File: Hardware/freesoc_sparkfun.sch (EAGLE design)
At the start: 94 parts, among them J1 POWER_JACKPTH, U1 CY8C5868AXI-LP035, U2 MIC5219 5V, U3 MIC5219 3.3V, U7 CY8C5868LTI-LP039, Y1 32.768kHz

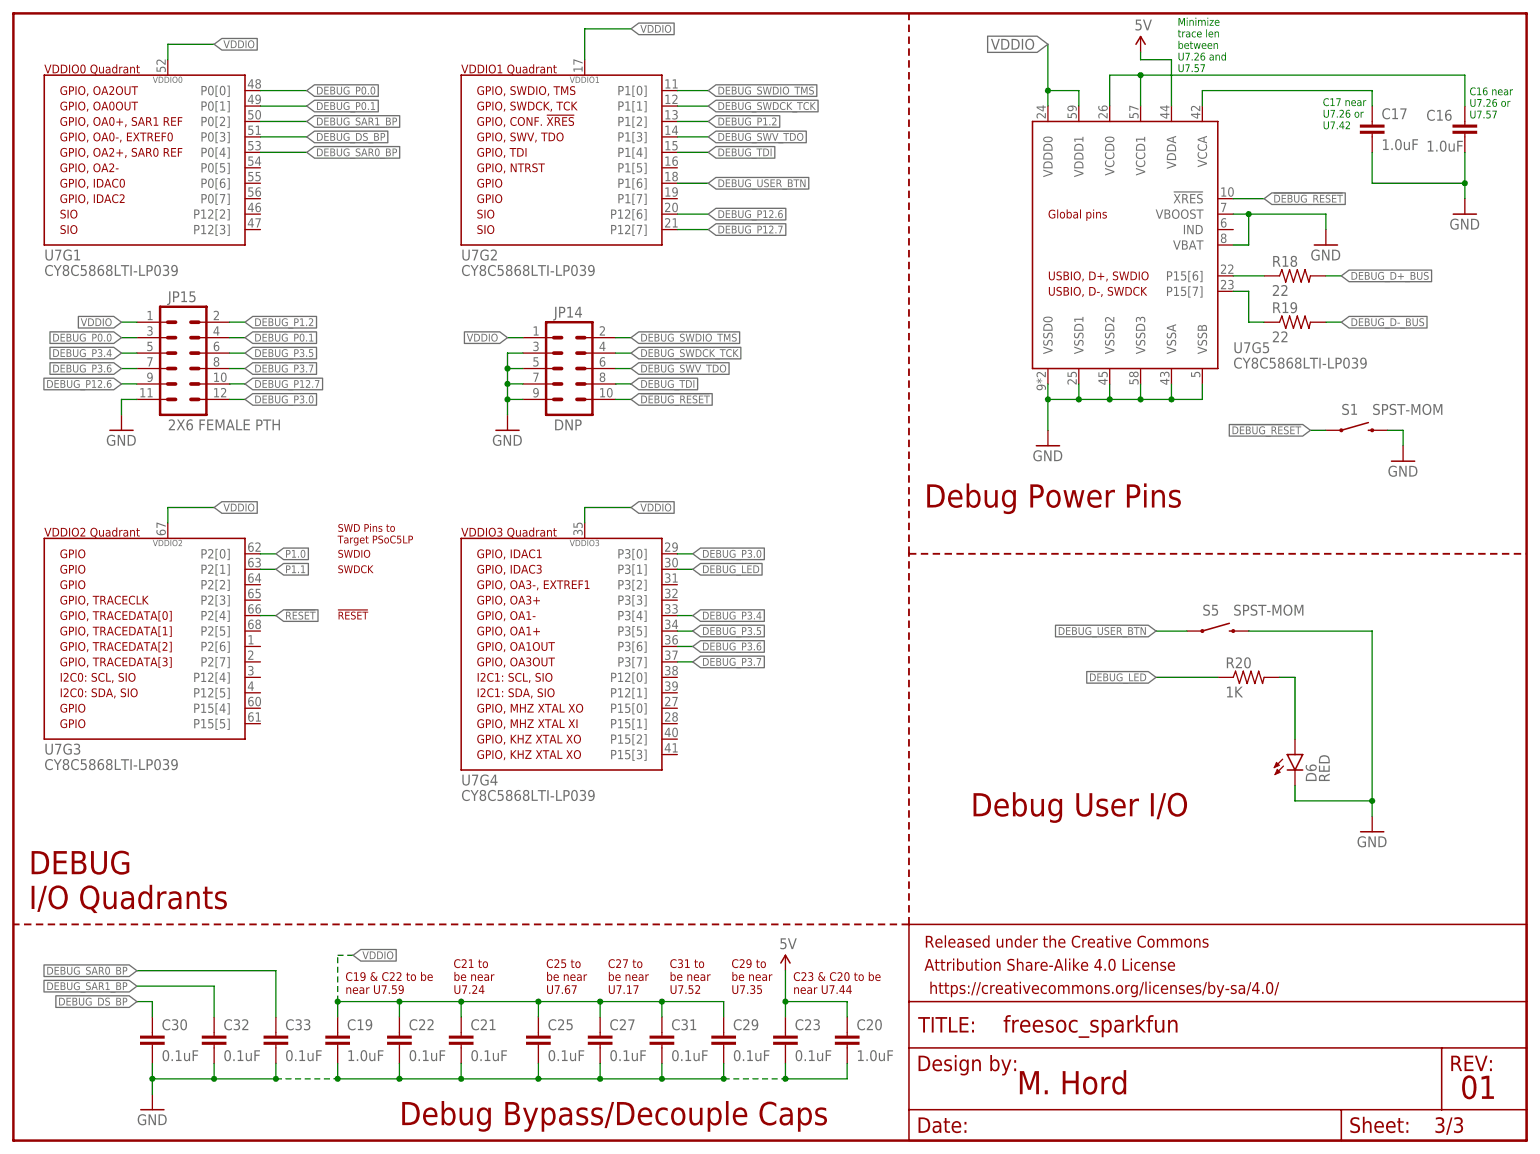
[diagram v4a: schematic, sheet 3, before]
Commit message: Files changed after v01 feedback, to add kitprog ID pins
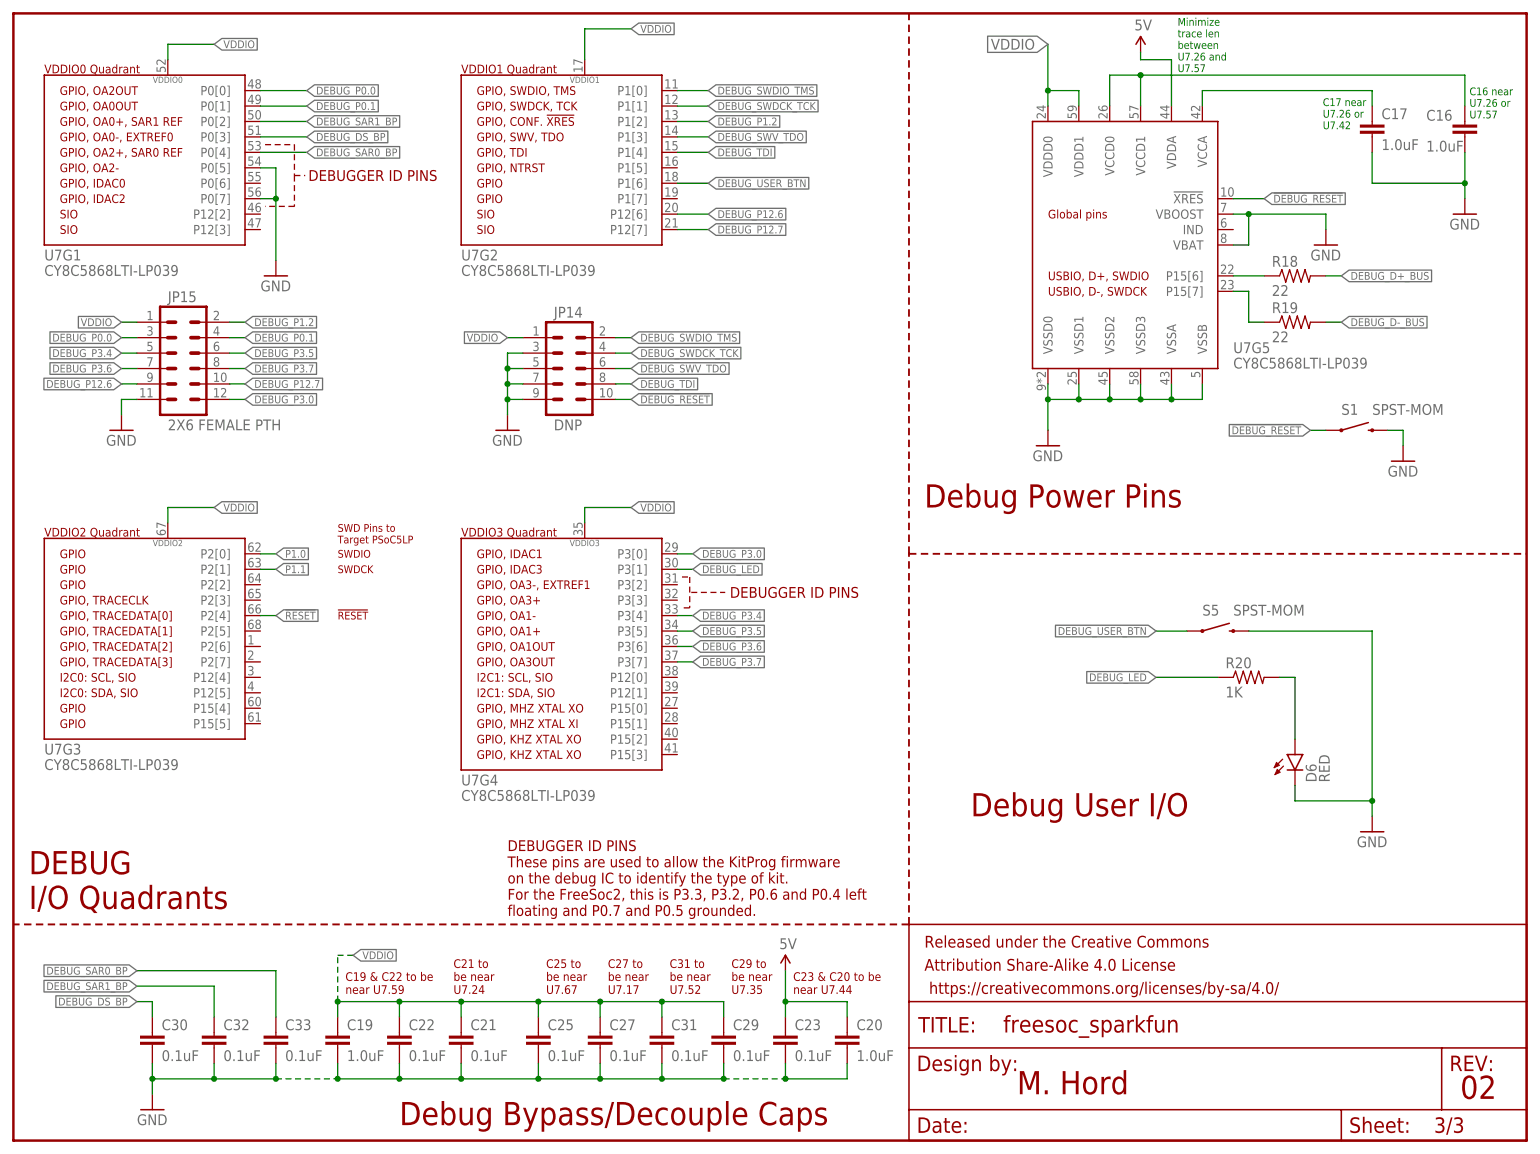
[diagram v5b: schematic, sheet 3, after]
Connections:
- net GND: now also U7G1.P0[5], U7G1.P0[7]
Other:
- note added: "02"
- note added: "DEBUGGER ID PINS"
- note added: "DEBUGGER ID PINS These pins are used to allow the KitProg firmware on the debug IC to identify the type of kit. For the FreeSoc2, this is P3.3, P3.2, P0.6 and P0.4 left floating and P0.7 and P0.5 grounded."
- note removed: "01"
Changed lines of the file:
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@@
 <part name="LOGO2" library="SparkFun-Aesthetics" deviceset="OSHW-LOGO" device="S"/>
 <part name="GND12" library="SparkFun-Aesthetics" deviceset="GND" device=""/>
+<part name="GND28" library="SparkFun-Aesthetics" deviceset="GND" device=""/>
 </parts>
 <sheets>
@@
 <text x="113.792" y="31.496" size="2.54" layer="94">Port 12 (SIO pins)</text>
 <text x="165.1" y="7.62" size="3.81" layer="94">M. Hord</text>
-<text x="237.998" y="6.858" size="3.81" layer="94">01</text>
+<text x="237.998" y="6.858" size="3.81" layer="94">02</text>
 <text x="1.016" y="1.27" size="1.778" layer="94">Developed with help from Jon Moeller
 and Cypress Semiconductor</text>
@@
 <wire x1="124.46" y1="185.42" x2="124.46" y2="109.22" width="0.3048" layer="94" style="longdash"/>
 <text x="165.1" y="7.62" size="3.81" layer="94">M. Hord</text>
-<text x="237.998" y="6.858" size="3.81" layer="94">01</text>
+<text x="237.998" y="6.858" size="3.81" layer="94">02</text>
 <text x="58.42" y="12.7" size="3.81" layer="94">Power Supply
 2.5V - 12V</text>
@@
 <wire x1="147.32" y1="96.52" x2="248.92" y2="96.52" width="0.3048" layer="94" style="longdash"/>
 <text x="165.1" y="7.62" size="3.81" layer="94">M. Hord</text>
-<text x="237.998" y="6.858" size="3.81" layer="94">01</text>
+<text x="237.998" y="6.858" size="3.81" layer="94">02</text>
+<wire x1="109.982" y1="92.71" x2="111.252" y2="92.71" width="0.1524" layer="94" style="shortdash"/>
+<wire x1="111.252" y1="92.71" x2="111.252" y2="87.63" width="0.1524" layer="94" style="shortdash"/>
+<wire x1="111.252" y1="87.63" x2="109.982" y2="87.63" width="0.1524" layer="94" style="shortdash"/>
+<wire x1="111.506" y1="90.17" x2="117.094" y2="90.17" width="0.1524" layer="94" style="shortdash"/>
+<text x="117.856" y="90.17" size="1.778" layer="94" align="center-left">DEBUGGER ID PINS</text>
+<wire x1="41.402" y1="163.83" x2="46.228" y2="163.83" width="0.1524" layer="94" style="shortdash"/>
+<wire x1="46.228" y1="163.83" x2="46.228" y2="158.75" width="0.1524" layer="94" style="shortdash"/>
+<wire x1="46.228" y1="158.75" x2="46.228" y2="153.67" width="0.1524" layer="94" style="shortdash"/>
+<wire x1="46.228" y1="153.67" x2="41.402" y2="153.67" width="0.1524" layer="94" style="shortdash"/>
+<wire x1="46.228" y1="158.75" x2="48.006" y2="158.75" width="0.1524" layer="94" style="shortdash"/>
+<text x="48.514" y="158.75" size="1.778" layer="94" align="center-left">DEBUGGER ID PINS</text>
+<text x="81.28" y="43.18" size="1.778" layer="94" align="center-left">DEBUGGER ID PINS
+These pins are used to allow the KitProg firmware
+on the debug IC to identify the type of kit.
+For the FreeSoc2, this is P3.3, P3.2, P0.6 and P0.4 left
+floating and P0.7 and P0.5 grounded.</text>
 </plain>
 <instances>
@@
 </instance>
 <instance part="GND12" gate="1" x="228.6" y="111.76"/>
+<instance part="GND28" gate="1" x="43.18" y="142.24"/>
 </instances>
 <busses>
@@
 <junction x="116.84" y="10.16"/>
 </segment>
-</net>
+<segment>
+<pinref part="U7" gate="G1" pin="P0[5]"/>
+<wire x1="40.64" y1="160.02" x2="43.18" y2="160.02" width="0.1524" layer="91"/>
+<wire x1="43.18" y1="160.02" x2="43.18" y2="154.94" width="0.1524" layer="91"/>
+<pinref part="U7" gate="G1" pin="P0[7]"/>
+<wire x1="43.18" y1="154.94" x2="40.64" y2="154.94" width="0.1524" layer="91"/>
+<wire x1="43.18" y1="154.94" x2="43.18" y2="144.78" width="0.1524" layer="91"/>
+<junction x="43.18" y="154.94"/>
+<pinref part="GND28" gate="1" pin="GND"/>
+</segment>
+</net>

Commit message: Changes for v02 in, review
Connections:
- net !RESET: now also U7G3.P12[4]; no longer U7G3.P2[4]
- net P1.0: now also U7G1.P12[2]; no longer U7G3.P2[0]
- net P1.1: now also U7G1.P12[3]; no longer U7G3.P2[1]
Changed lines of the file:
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@@
 <sheet>
 <plain>
-<text x="53.34" y="99.822" size="1.27" layer="94" align="center-left">SWD Pins to
+<text x="55.88" y="145.542" size="1.27" layer="94" align="center-left">SWD Pins to
 Target PSoC5LP</text>
-<text x="53.34" y="96.52" size="1.27" layer="94" align="center-left">SWDIO</text>
-<text x="53.34" y="93.98" size="1.27" layer="94" align="center-left">SWDCK</text>
-<text x="53.34" y="86.36" size="1.27" layer="94" align="center-left">!RESET</text>
+<text x="55.88" y="152.4" size="1.27" layer="94" align="center-left">SWDIO</text>
+<text x="55.88" y="149.86" size="1.27" layer="94" align="center-left">SWDCK</text>
+<text x="53.34" y="76.2" size="1.27" layer="94" align="center-left">!RESET</text>
 <text x="54.61" y="24.13" size="1.4224" layer="94">C19 &amp; C22 to be
 near U7.59</text>
@@
 For the FreeSoc2, this is P3.3, P3.2, P0.6 and P0.4 left
 floating and P0.7 and P0.5 grounded.</text>
+<text x="53.34" y="79.502" size="1.27" layer="94" align="center-left">SWD Pins to
+Target PSoC5LP</text>
 </plain>
 <instances>
@@
 <net name="P1.0" class="0">
 <segment>
-<pinref part="U7" gate="G3" pin="P2[0]"/>
-<wire x1="40.64" y1="96.52" x2="43.18" y2="96.52" width="0.1524" layer="91"/>
-<label x="43.18" y="96.52" size="1.27" layer="95" xref="yes"/>
+<label x="45.72" y="152.4" size="1.27" layer="95" xref="yes"/>
+<pinref part="U7" gate="G1" pin="P12[2]"/>
+<wire x1="40.64" y1="152.4" x2="45.72" y2="152.4" width="0.1524" layer="91"/>
 </segment>
 </net>
 <net name="P1.1" class="0">
 <segment>
-<pinref part="U7" gate="G3" pin="P2[1]"/>
-<wire x1="40.64" y1="93.98" x2="43.18" y2="93.98" width="0.1524" layer="91"/>
-<label x="43.18" y="93.98" size="1.27" layer="95" xref="yes"/>
+<label x="45.72" y="149.86" size="1.27" layer="95" xref="yes"/>
+<pinref part="U7" gate="G1" pin="P12[3]"/>
+<wire x1="40.64" y1="149.86" x2="45.72" y2="149.86" width="0.1524" layer="91"/>
 </segment>
 </net>
 <net name="!RESET" class="0">
 <segment>
-<pinref part="U7" gate="G3" pin="P2[4]"/>
-<wire x1="40.64" y1="86.36" x2="43.18" y2="86.36" width="0.1524" layer="91"/>
-<label x="43.18" y="86.36" size="1.27" layer="95" xref="yes"/>
-</segment>
-</net>
+<label x="43.18" y="76.2" size="1.27" layer="95" xref="yes"/>
+<pinref part="U7" gate="G3" pin="P12[4]"/>
+<wire x1="43.18" y1="76.2" x2="40.64" y2="76.2" width="0.1524" layer="91"/>
+</segment>
+</net>

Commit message: ready for protos v02
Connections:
- removed net P1.5: U1G2.P1[5]
- removed net P1.6: U1G2.P1[6]
- removed net P1.7: U1G2.P1[7]
- net GND: now also JP10.1; no longer JP10.2
- net VDDIO: now also JP10.2; no longer JP10.1
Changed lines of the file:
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@@
 <layer number="254" name="cooling" color="7" fill="1" visible="no" active="yes"/>
 </layers>
-<schematic xreflabel="%F%N/%S" xrefpart="1_/%S.%C%R">
+<schematic xreflabel="%F%N/%S" xrefpart="/%S.%C%R">
 <attributes>
 </attributes>
@@
 </segment>
 <segment>
-<pinref part="JP10" gate="G$1" pin="1"/>
-<wire x1="132.08" y1="25.4" x2="129.54" y2="25.4" width="0.1524" layer="91"/>
-<label x="129.54" y="25.4" size="1.27" layer="95" rot="R180" xref="yes"/>
+<pinref part="JP10" gate="G$1" pin="2"/>
+<wire x1="132.08" y1="22.86" x2="129.54" y2="22.86" width="0.1524" layer="91"/>
+<label x="129.54" y="22.86" size="1.27" layer="95" rot="R180" xref="yes"/>
 </segment>
 </net>
@@
 </segment>
 <segment>
-<pinref part="JP10" gate="G$1" pin="2"/>
-<wire x1="132.08" y1="22.86" x2="119.38" y2="22.86" width="0.1524" layer="91"/>
-<wire x1="119.38" y1="22.86" x2="119.38" y2="7.62" width="0.1524" layer="91"/>
+<wire x1="119.38" y1="25.4" x2="119.38" y2="7.62" width="0.1524" layer="91"/>
 <pinref part="GND20" gate="1" pin="GND"/>
+<pinref part="JP10" gate="G$1" pin="1"/>
+<wire x1="132.08" y1="25.4" x2="119.38" y2="25.4" width="0.1524" layer="91"/>
 </segment>
 <segment>
@@
 </segment>
 </net>
-<net name="P1.5" class="0">
-<segment>
-<pinref part="U1" gate="G2" pin="P1[5]"/>
-<wire x1="43.18" y1="73.66" x2="48.26" y2="73.66" width="0.1524" layer="91"/>
-<label x="48.26" y="73.66" size="1.27" layer="95" xref="yes"/>
-</segment>
-</net>
-<net name="P1.6" class="0">
-<segment>
-<pinref part="U1" gate="G2" pin="P1[6]"/>
-<wire x1="43.18" y1="71.12" x2="48.26" y2="71.12" width="0.1524" layer="91"/>
-<label x="48.26" y="71.12" size="1.27" layer="95" xref="yes"/>
-</segment>
-</net>
-<net name="P1.7" class="0">
-<segment>
-<pinref part="U1" gate="G2" pin="P1[7]"/>
-<wire x1="43.18" y1="68.58" x2="48.26" y2="68.58" width="0.1524" layer="91"/>
-<label x="48.26" y="68.58" size="1.27" layer="95" xref="yes"/>
-</segment>
-</net>

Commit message: Up to V02, checklist and peer review completed
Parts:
- removed J1: POWER_JACKPTH, SparkFun-Connectors:POWER_JACKPTH
- added JP18: POWER_JACKPTH_LOCK, SparkFun-Connectors:POWER_JACKPTH_LOCK
- FRAME1: value FRAME-LETTER -> (none); DESIGNER (none) -> M. Hord; VERSION (none) -> v02
- FRAME2, FRAME3: value FRAME-LETTER -> (none)
- JP11, JP12, JP15, JP8, JP9: value 2X6 FEMALE PTH -> 2X6 FEMALE
- S3, S4: device SparkFun-Electromechanical:SWITCH-SPDTPTH -> SparkFun-Electromechanical:SWITCH-SPDTPTH_LOCK
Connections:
- net GND: now also JP18.GND, JP18.GNDBREAK; no longer J1.GND, J1.GNDBREAK
- net N$13: now also JP18.PWR; no longer J1.PWR
